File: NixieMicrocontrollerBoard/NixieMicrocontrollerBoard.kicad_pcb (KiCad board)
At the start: 2 copper layers, 48.3 x 49.5 mm, 12 parts, among them IC1 ATMEGA328-P, P1 CONN_01X03, P2 GPS_Header, P3 SD_Header, P4 Nixie_Header, Y1 16MHz

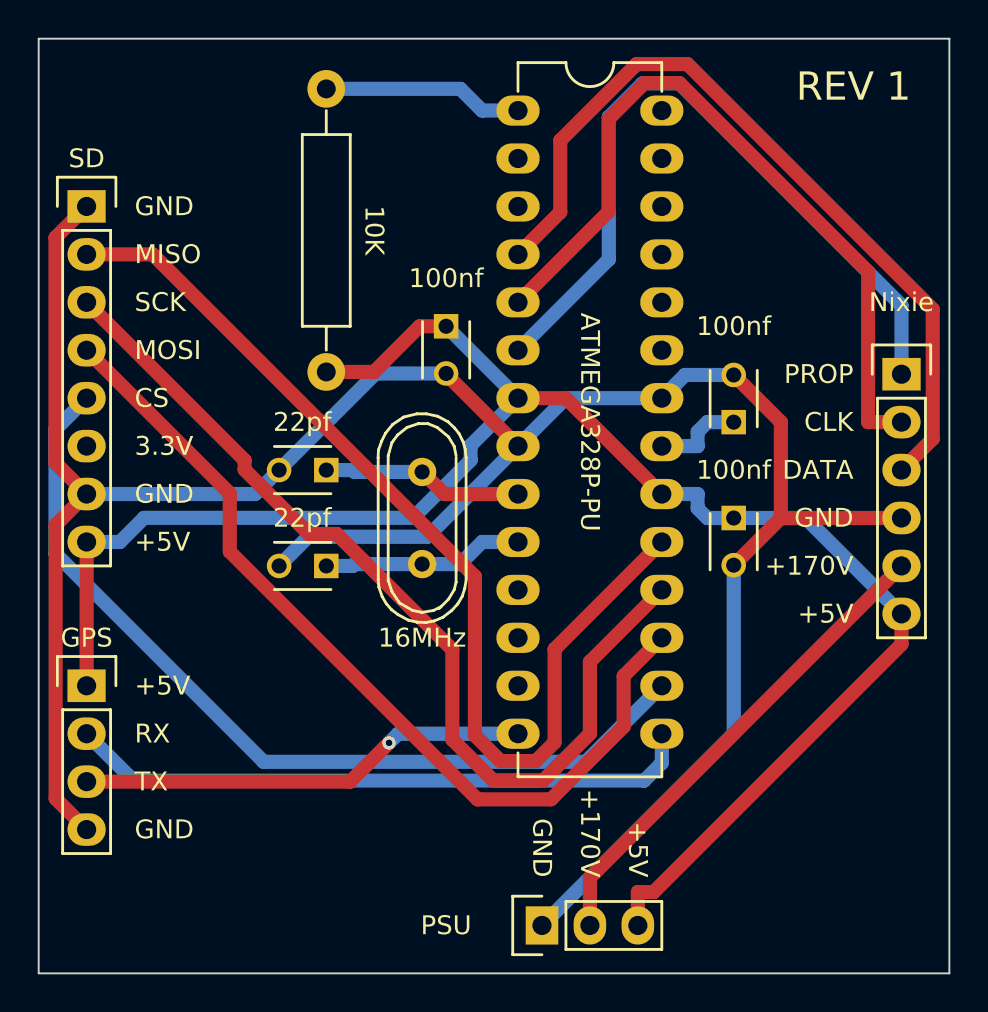
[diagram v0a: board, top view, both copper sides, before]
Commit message: Fixes up the microcontroller board, and adds a library to drive the Nixie boards
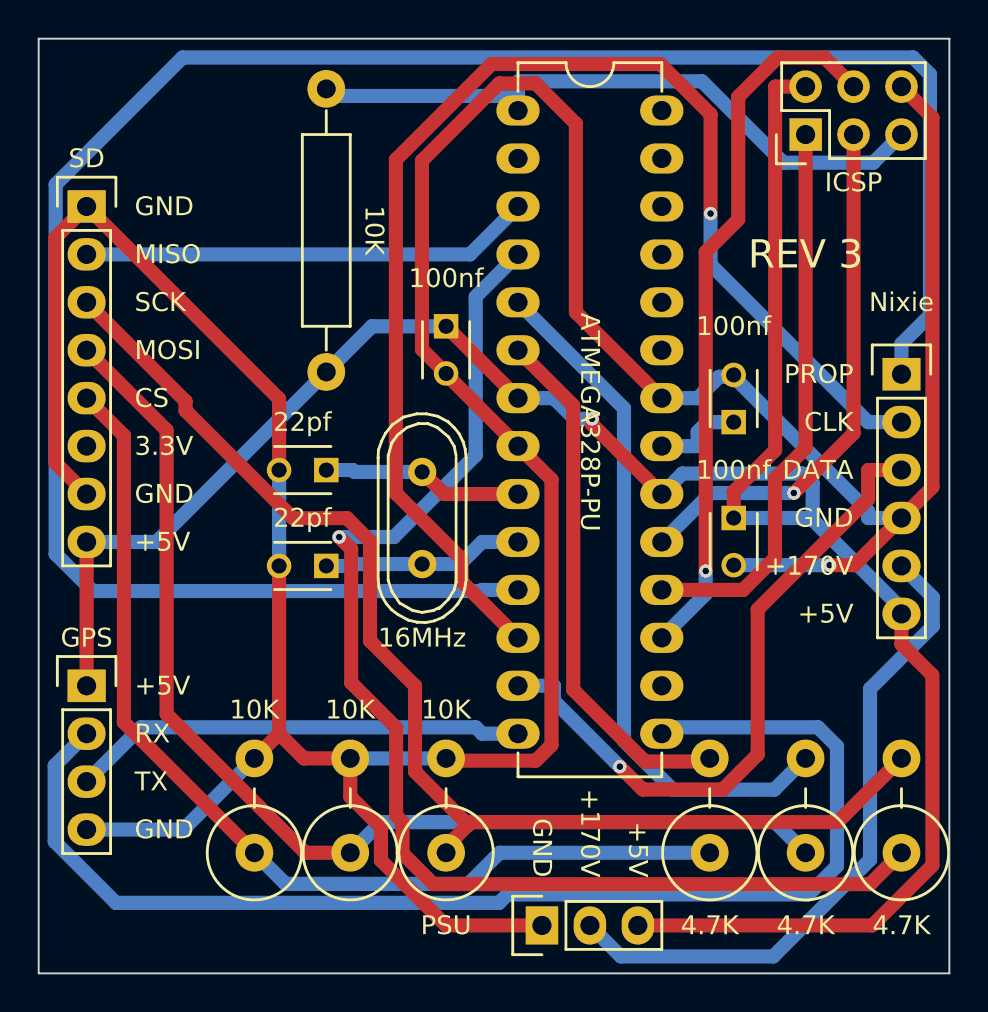
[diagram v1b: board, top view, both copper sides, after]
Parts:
- added P5: ICSP, Pin_Headers:Pin_Header_Straight_2x03, F.Cu at (179.1, 96.5)
- added R2: 4.7K, Resistors_ThroughHole:Resistor_Vertical_RM5mm, F.Cu at (184.2, 132.1)
- added R3: 4.7K, Resistors_ThroughHole:Resistor_Vertical_RM5mm, F.Cu at (179.1, 132.1)
- added R4: 4.7K, Resistors_ThroughHole:Resistor_Vertical_RM5mm, F.Cu at (174.0, 132.1)
- added R5: 10K, Resistors_ThroughHole:Resistor_Vertical_RM5mm, F.Cu at (160.0, 132.1)
- added R6: 10K, Resistors_ThroughHole:Resistor_Vertical_RM5mm, F.Cu at (154.9, 132.1)
- added R7: 10K, Resistors_ThroughHole:Resistor_Vertical_RM5mm, F.Cu at (149.9, 132.1)
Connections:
- P3 pad 2: Net-(IC1-Pad19) -> Net-(IC1-Pad3)
- P3 pad 3: Net-(IC1-Pad18) -> Net-(P3-Pad3)
- P3 pad 4: Net-(IC1-Pad17) -> Net-(P3-Pad4)
- P3 pad 5: Net-(IC1-Pad16) -> Net-(P3-Pad5)
- P4 pad 1: Net-(IC1-Pad6) -> Net-(IC1-Pad11)
- P4 pad 2: Net-(IC1-Pad5) -> Net-(IC1-Pad12)
- P4 pad 3: Net-(IC1-Pad4) -> Net-(IC1-Pad13)
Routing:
- net Net-(IC1-Pad11): track 0.00 -> 110.9 mm
- net GND: track 133.0 -> 204.2 mm, vias 0 -> 1
- net Net-(IC1-Pad12): track 0.00 -> 69.4 mm, vias 0 -> 1
- net Net-(P3-Pad3): track 0.00 -> 64.1 mm
- net Net-(P3-Pad4): track 0.00 -> 59.3 mm
- net Net-(P3-Pad5): track 0.00 -> 53.3 mm
- net Net-(IC1-Pad16): track 47.3 -> 0.00 mm
- net Net-(IC1-Pad13): track 0.00 -> 35.5 mm, vias 0 -> 1
- net Net-(IC1-Pad15): track 33.4 -> 66.2 mm
- net VCC: track 95.1 -> 124.7 mm, vias 0 -> 1
- net Net-(IC1-Pad19): track 54.2 -> 28.4 mm, vias 0 -> 1
- net Net-(IC1-Pad1): track 10.6 -> 34.6 mm
- net Net-(IC1-Pad3): track 0.00 -> 23.9 mm
- net Net-(IC1-Pad4): track 43.0 -> 66.6 mm, vias 0 -> 1
- net Net-(IC1-Pad18): track 50.5 -> 29.8 mm
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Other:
- board text added: "4.7K"
- board text added: "ICSP"
- board text added: "REV 3"
- board text removed: "REV 1"

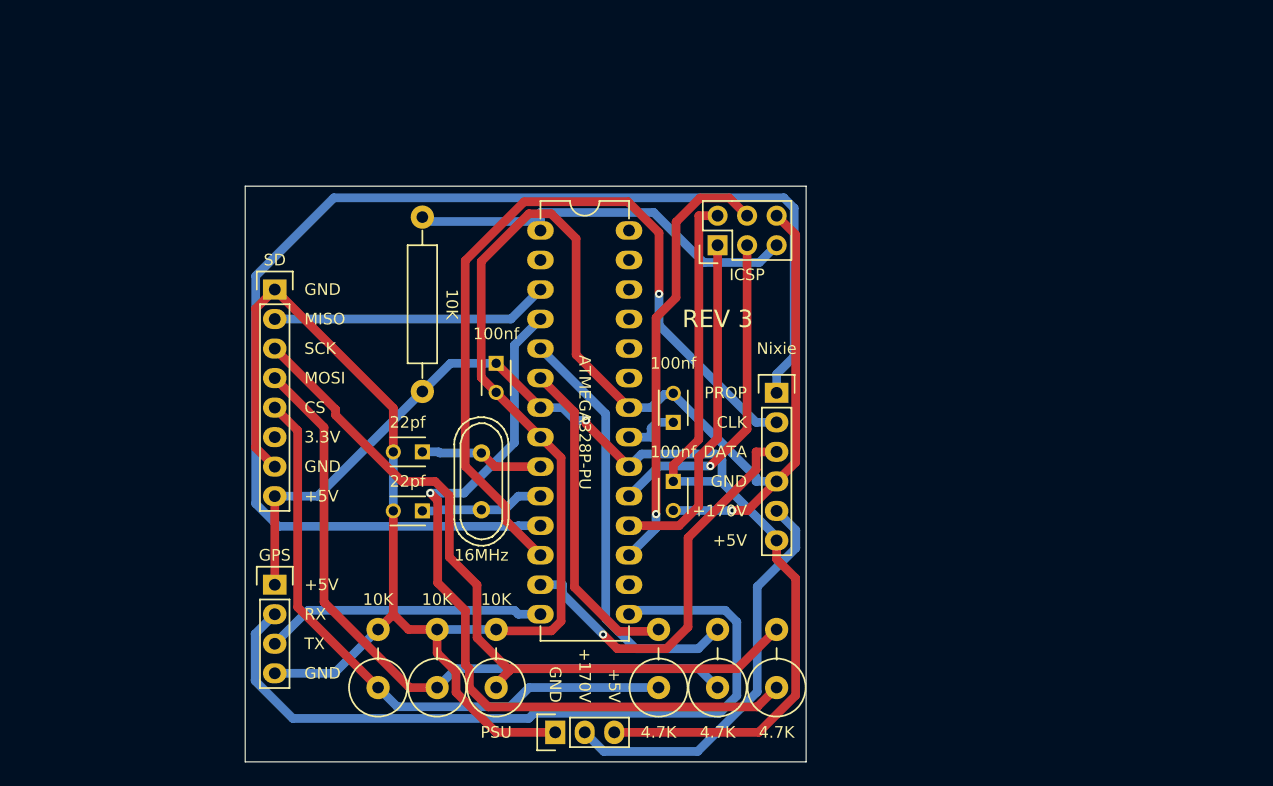
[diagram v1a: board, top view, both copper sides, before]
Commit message: Updates NixieMicrocontrollerBoard to include power circuits, and all of the changes I made to the breadboarded circuit yesterday
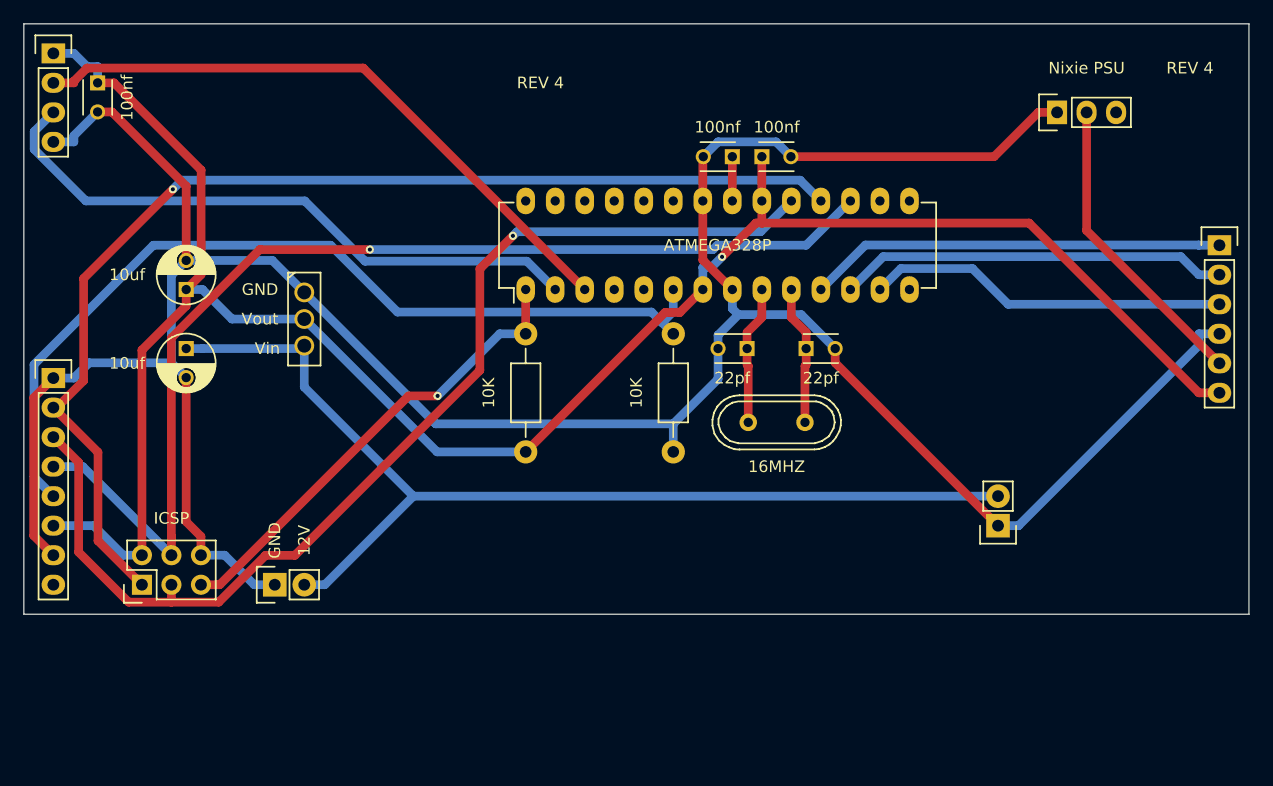
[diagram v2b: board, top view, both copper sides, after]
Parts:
- removed R3, R4: 4.7K, Resistors_ThroughHole:Resistor_Vertical_RM5mm
- removed R5, R6, R7: 10K, Resistors_ThroughHole:Resistor_Vertical_RM5mm
- added C6: 10uf, Capacitors_ThroughHole:C_Radial_D5_L11_P2.5, F.Cu at (133.3, 105.4)
- added C7: 10uf, Capacitors_ThroughHole:C_Radial_D5_L11_P2.5, F.Cu at (133.3, 100.3)
- added P6: CONN_01X02, Pin_Headers:Pin_Header_Straight_1x02, F.Cu at (203.2, 120.7)
- added P7: CONN_01X02, Pin_Headers:Pin_Header_Straight_1x02, F.Cu at (141.0, 125.7)
- added U1: LD1117S12CTR, TO_SOT_Packages_THT:SOT126_SOT32_Housing_Vertical, F.Cu at (143.5, 102.9)
- IC1: footprint BetterDIP:DIP-28_W7.62mm_LongPads -> Housings_DIP:DIP-28_W7.62mm_LongPads
- R1: footprint Resistors_ThroughHole:Resistor_Horizontal_RM15mm -> Resistors_ThroughHole:Resistor_Horizontal_RM10mm
- R2: value 4.7K -> 10K; footprint Resistors_ThroughHole:Resistor_Vertical_RM5mm -> Resistors_ThroughHole:Resistor_Horizontal_RM10mm
- moved P1 68.6 mm to (208.3, 85.1)
- moved C2 60.2 mm to (125.7, 82.5)
- moved P5 57.5 mm to (129.5, 125.7)
- moved P2 49.5 mm to (121.9, 80.0)
- moved P4 40.2 mm to (222.2, 96.5)
- moved C4 35.9 mm to (186.7, 105.4), turned to 0 degrees
- moved C5 29.3 mm to (181.6, 105.4)
- moved C1 29.0 mm to (182.9, 88.9), turned to 0 degrees
- moved Y1 25.9 mm to (184.2, 111.8), turned to 0 degrees
- moved C3 23.4 mm to (180.3, 88.9), turned to 180 degrees
- moved P3 20.5 mm to (121.9, 108.0)
- moved R2 19.9 mm to (175.3, 114.3)
- moved R1 9.25 mm to (162.6, 104.1)
- moved IC1 5.24 mm to (162.6, 100.3), turned to 90 degrees
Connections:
- P1 pad 3: VCC -> Net-(P1-Pad3)
- P2 pad 2: Net-(IC1-Pad15) -> Net-(IC1-Pad3)
- P2 pad 3: Net-(IC1-Pad14) -> Net-(IC1-Pad2)
- P3 pad 2: Net-(IC1-Pad3) -> Net-(IC1-Pad18)
- P3 pad 3: Net-(P3-Pad3) -> Net-(IC1-Pad19)
- P3 pad 4: Net-(P3-Pad4) -> Net-(IC1-Pad17)
- P3 pad 5: Net-(P3-Pad5) -> Net-(IC1-Pad6)
- P3 pad 6: Net-(P3-Pad6) -> VCC
- P3 pad 8: VCC -> Net-(P3-Pad8)
- R2 pad 1: Net-(IC1-Pad4) -> GND
- R2 pad 2: Net-(P3-Pad3) -> Net-(IC1-Pad6)
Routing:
- net Net-(C6-Pad1): track 0.00 -> 89.8 mm
- net Net-(IC1-Pad11): track 110.9 -> 35.9 mm
- net Net-(IC1-Pad18): track 29.8 -> 98.3 mm, vias 0 -> 1
- net Net-(IC1-Pad4): track 66.6 -> 0.00 mm, vias 1 -> 0
- net Net-(IC1-Pad19): track 28.4 -> 94.8 mm
- net Net-(IC1-Pad15): track 66.2 -> 0.00 mm
- net Net-(P3-Pad3): track 64.1 -> 0.00 mm
- net Net-(P3-Pad4): track 59.3 -> 0.00 mm
- net Net-(IC1-Pad17): track 37.9 -> 95.3 mm
- net Net-(IC1-Pad2): track 0.00 -> 53.7 mm
- net Net-(P3-Pad5): track 53.3 -> 0.00 mm
- net VCC: track 124.7 -> 177.3 mm
- net Net-(IC1-Pad6): track 28.1 -> 77.7 mm
- net GND: track 204.2 -> 250.4 mm, vias 1 -> 0
- net Net-(IC1-Pad5): track 36.9 -> 0.00 mm
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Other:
- board size 48.3 x 49.5 mm -> 105.4 x 50.8 mm
- net class Default: trace_width 0.75 -> 1.016
- board text added: "10uf"
- board text added: "12V"
- board text added: "16MHZ"
- board text added: "ATMEGA328P"
- board text added: "Nixie PSU"
- board text added: "REV 4"
- board text added: "Vin"
- board text added: "Vout"
- board text removed: "+170V"
- board text removed: "+5V"
- board text removed: "16MHz"
- board text removed: "3.3V"
- board text removed: "4.7K"
- board text removed: "ATMEGA328P-PU"
- board text removed: "CLK"
- board text removed: "CS"
- board text removed: "DATA"
- board text removed: "GPS"
- board text removed: "MISO"
- board text removed: "MOSI"
- board text removed: "Nixie"
- board text removed: "PROP"
- board text removed: "PSU"
- board text removed: "REV 3"
- board text removed: "RX"
- board text removed: "SCK"
- board text removed: "SD"
- board text removed: "TX"

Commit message: Makes the board more heatsink-friendly
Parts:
- moved C6 19.2 mm to (152.4, 102.9)
- moved C7 19.2 mm to (152.4, 97.8)
- moved U1 4.07 mm to (140.3, 100.3)
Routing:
- net Net-(IC1-Pad12): track 33.6 -> 51.5 mm
- net VCC: track 177.3 -> 195.1 mm, vias 1 -> 2
- net Net-(IC1-Pad11): track 35.9 -> 52.1 mm
- net Net-(IC1-Pad13): track 31.2 -> 44.4 mm
- net Net-(IC1-Pad6): track 77.7 -> 67.1 mm
- net Net-(IC1-Pad1): track 40.7 -> 50.7 mm, vias 1 -> 0
- net Net-(C6-Pad1): track 89.8 -> 97.9 mm
- net Net-(IC1-Pad19): track 94.8 -> 100.9 mm, vias 1 -> 0
- net Net-(IC1-Pad2): track 53.7 -> 49.5 mm
- net Net-(IC1-Pad18): track 98.3 -> 101.7 mm, vias 1 -> 0
- net Net-(IC1-Pad17): track 95.3 -> 92.5 mm, vias 1 -> 0
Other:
- board text added: "REV 5"
- board text removed: "REV 4"
